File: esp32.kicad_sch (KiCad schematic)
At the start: 30 parts, among them J10 Conn_01x02, J5 TC2030-IDC, J6 Conn_01x04, J8 USB_C_Receptacle_USB2.0, J9 Conn_01x04, SW1 GT-TC029B-H025-L1N, SW2 GT-TC029B-H025-L1N, U11 RT9080-33GJ5, U12 ESP32-S3-WROOM-1, Y1 32.768kHz

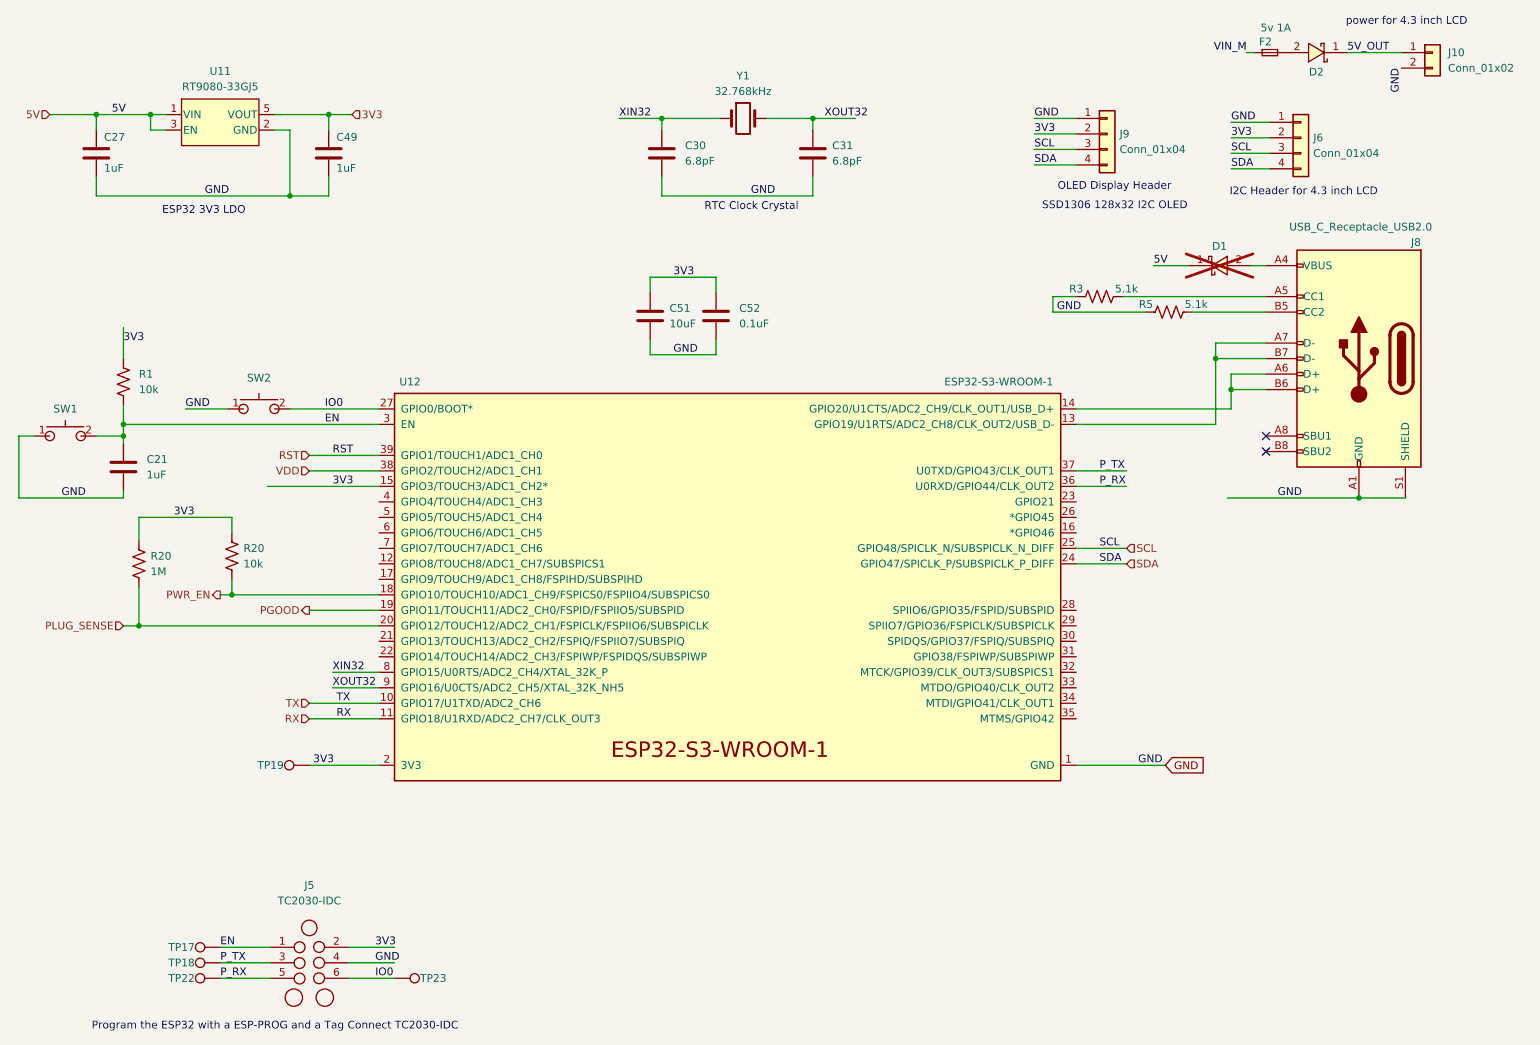
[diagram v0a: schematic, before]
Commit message: added sda and scl puulups
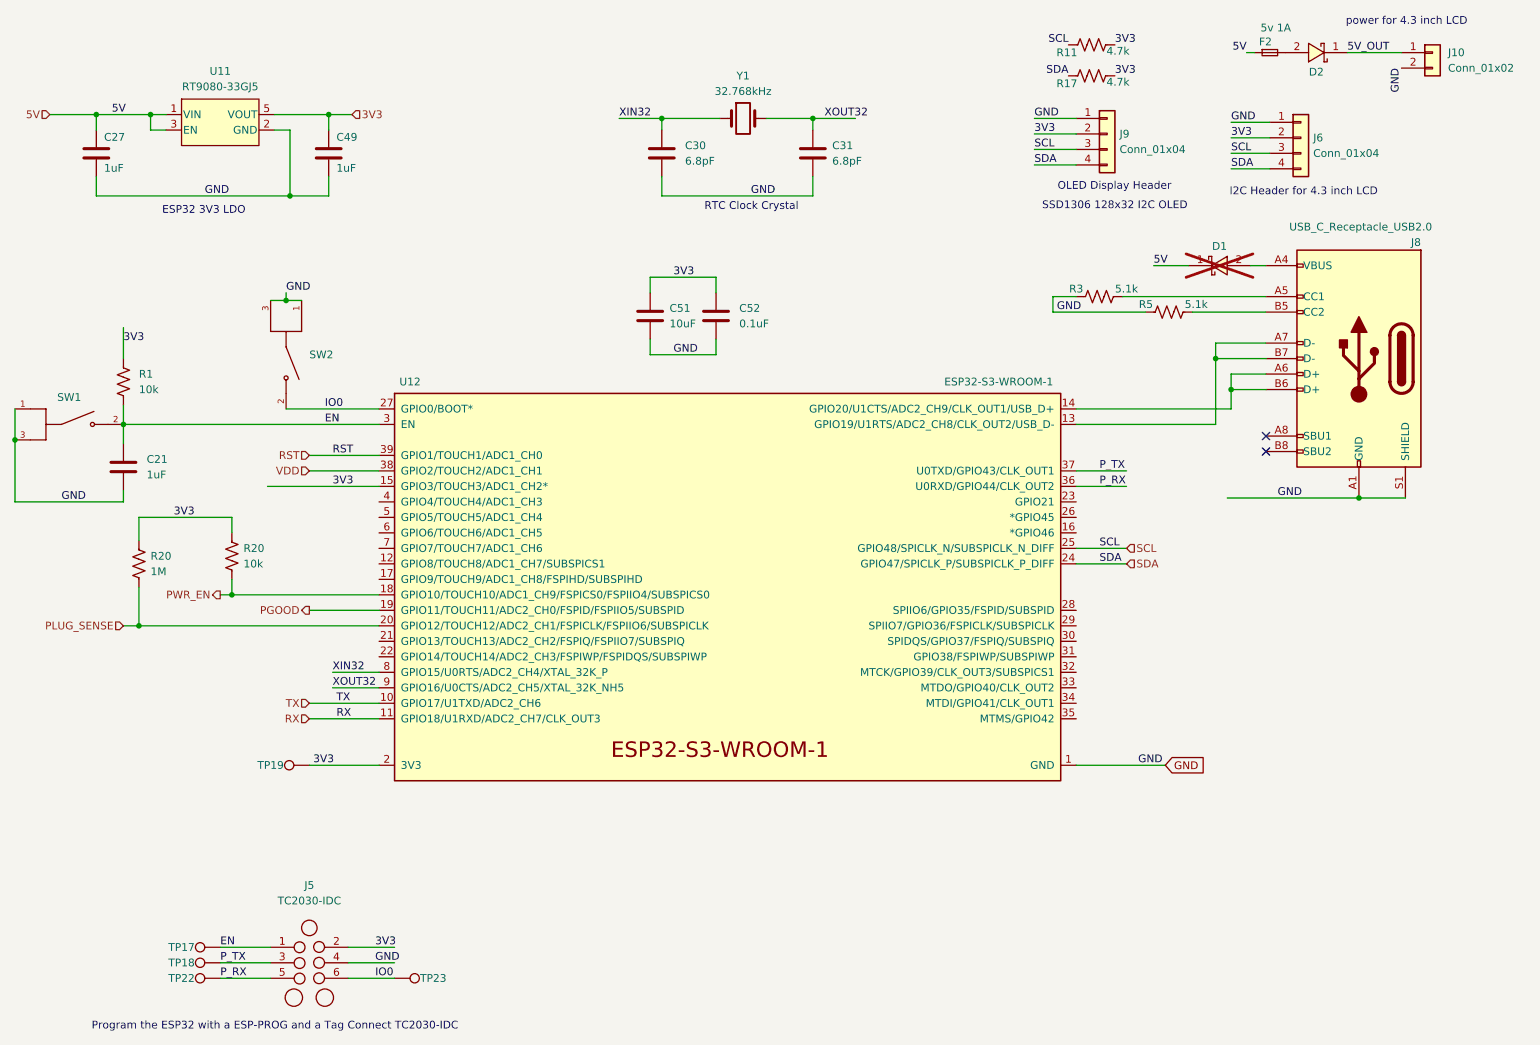
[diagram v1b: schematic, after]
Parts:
- added R11, R17: 4.7k, Resistor_SMD:R_0402_1005Metric, symbol Device:R_US
- SW1, SW2: footprint bitaxe:SW_CS1213AGF260_CRS -> bitaxe:SW_TL3340AF160QG; symbol bitaxe:GT-TC029B-H025-L1N -> TL3340AF160QG:TL3340AF160QG; AVAILABILITY (none) -> In Stock; DESCRIPTION (none) -> Tactile Switch SPST-NO Side Actuated Surface Mount, Right A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; MF (none) -> E-Switch; MP (none) -> TL3340AF160QG; PACKAGE (none) -> None; PRICE (none) -> None; PURCHASE-URL (none) -> https://pricing.snapeda.com/search/part/TL3340AF160QG/?ref=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
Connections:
- net VIN_M is gone; now on net 5V: F2.1
- net 3V3: now also R11.2, R17.2
- net GND: now also SW1.3, SW2.3
- net SCL: now also R11.1
- net SDA: now also R17.1
